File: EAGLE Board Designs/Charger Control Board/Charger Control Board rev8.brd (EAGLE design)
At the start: 86.4 x 101.6 mm, 120 parts, among them K1 RELAY_DPDT, K2 RELAY_DPDT, K3 RELAY_DPDT, U1 LOGICGATE_BUFFER, U100 MCP2562FD, U101 MCP2562FD, U2 ADM8316WBX30, U3 VOLTAGE_REGULATOR_MODULE_OKI-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

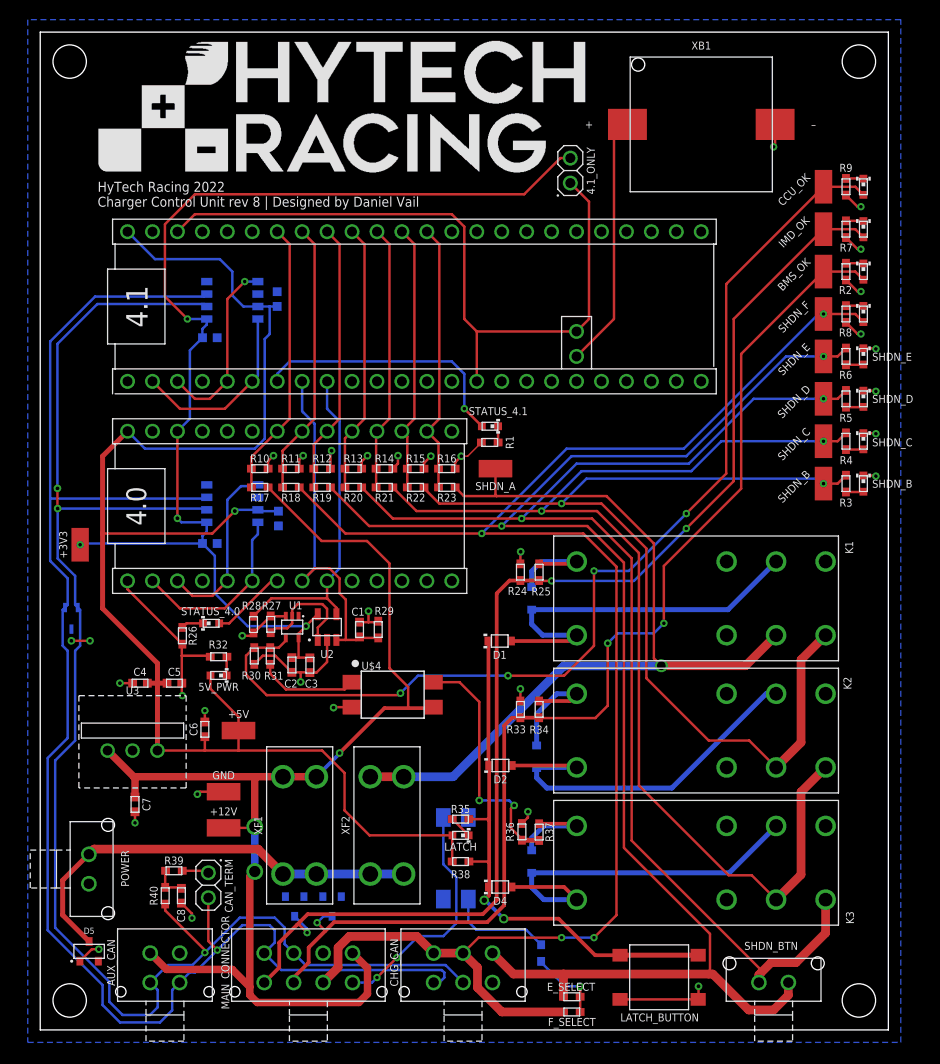
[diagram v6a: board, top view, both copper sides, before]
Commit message: Cleaned up silkscreen
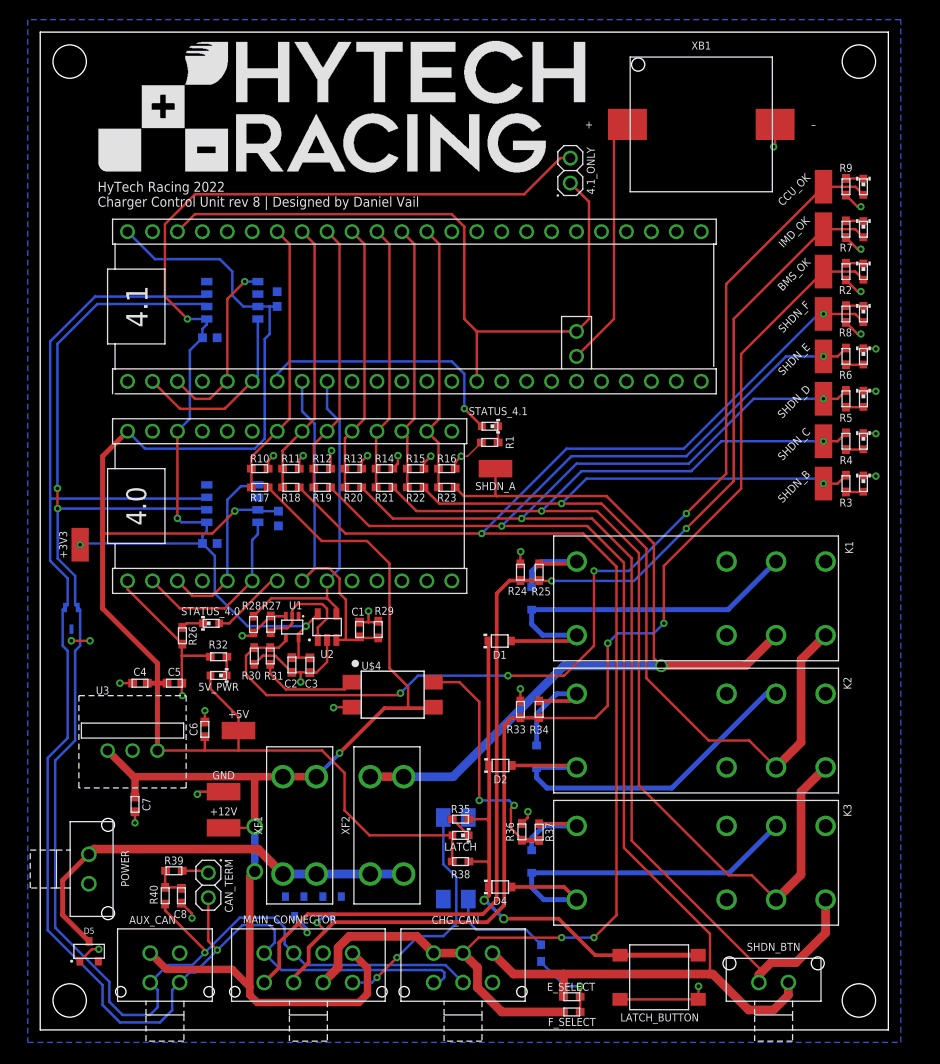
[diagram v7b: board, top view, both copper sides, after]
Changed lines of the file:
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@@
 <drawing>
 <settings>
-<setting alwaysvectorfont="no"/>
+<setting alwaysvectorfont="yes"/>
 <setting verticaltext="up"/>
 </settings>
@@
 <layer number="20" name="Dimension" color="24" fill="1" visible="yes" active="yes"/>
 <layer number="21" name="tPlace" color="7" fill="1" visible="yes" active="yes"/>
-<layer number="22" name="bPlace" color="7" fill="1" visible="no" active="yes"/>
+<layer number="22" name="bPlace" color="7" fill="1" visible="yes" active="yes"/>
 <layer number="23" name="tOrigins" color="15" fill="1" visible="yes" active="yes"/>
 <layer number="24" name="bOrigins" color="15" fill="1" visible="yes" active="yes"/>
 <layer number="25" name="tNames" color="7" fill="1" visible="yes" active="yes"/>
 <layer number="26" name="bNames" color="7" fill="1" visible="yes" active="yes"/>
-<layer number="27" name="tValues" color="7" fill="1" visible="yes" active="yes"/>
+<layer number="27" name="tValues" color="7" fill="1" visible="no" active="yes"/>
 <layer number="28" name="bValues" color="7" fill="1" visible="no" active="yes"/>
 <layer number="29" name="tStop" color="7" fill="3" visible="no" active="yes"/>
@@
 <attribute name="MOPN" value="77-VJ0603Y104JXQPBC" x="130.81" y="32.512" size="1.778" layer="28" rot="MR270" display="off"/>
 <attribute name="MPN" value="VJ0603Y104JXQPW1BC" x="130.81" y="32.512" size="1.778" layer="28" rot="MR270" display="off"/>
-<attribute name="NAME" x="25.92" y="74.422" size="0.8128" layer="26" font="vector" rot="MR270" align="bottom-center"/>
+<attribute name="NAME" x="25.134" y="74.422" size="0.8128" layer="26" font="vector" rot="MR90" align="bottom-center"/>
 <attribute name="TOLERANCE" value="5%" x="130.81" y="32.512" size="1.778" layer="28" rot="MR270" display="off"/>
 <attribute name="VOLTAGE" value="10V" x="130.81" y="32.512" size="1.778" layer="28" rot="MR270" display="off"/>
@@
 <attribute name="MOPN" value="710-885012206012" x="-92.3036" y="-47.2948" size="1.778" layer="27" rot="R270" display="off"/>
 <attribute name="MPN" value="885012206012" x="-92.3036" y="-47.2948" size="1.778" layer="27" rot="R270" display="off"/>
-<attribute name="NAME" x="14.744" y="11.6332" size="0.8128" layer="25" font="vector" rot="R90" align="bottom-center"/>
+<attribute name="NAME" x="14.2748" y="12.204" size="0.8128" layer="25" font="vector" rot="R180" align="bottom-center"/>
 <attribute name="TOLERANCE" value="10%" x="-92.3036" y="-47.2948" size="1.778" layer="27" rot="R270" display="off"/>
 <attribute name="VOLTAGE" value="10V" x="-92.3036" y="-47.2948" size="1.778" layer="27" rot="R270" display="off"/>
@@
 <attribute name="MANUFACTURER" value="MOLEX" x="-22.225" y="89.916" size="1.778" layer="27" rot="R180" display="off"/>
 <attribute name="MPN" value="430450814" x="-22.225" y="89.916" size="1.778" layer="27" rot="R180" display="off"/>
-<attribute name="NAME" x="19.2532" y="6.858" size="0.8128" layer="25" font="vector" rot="R90" align="bottom-center"/>
+<attribute name="NAME" x="25.4" y="10.8458" size="0.8128" layer="25" font="vector" align="bottom-center"/>
 </element>
 <element name="R25" library="HyTechDevices" package="0603-RES" value="RESISTOR_0603_22" x="50.8" y="46.609" smashed="yes" rot="R270">
@@
 <attribute name="MOPN" value="603-RC0603FR-0760R4L" x="119.4054" y="86.0552" size="1.778" layer="27" rot="R90" display="off"/>
 <attribute name="MPN" value="RC0603FR-0760R4L" x="119.4054" y="86.0552" size="1.778" layer="27" rot="R90" display="off"/>
-<attribute name="NAME" x="11.1506" y="13.6652" size="0.8128" layer="25" font="vector" rot="R270" align="bottom-center"/>
+<attribute name="NAME" x="11.9634" y="13.7668" size="0.8128" layer="25" font="vector" rot="R90" align="bottom-center"/>
 <attribute name="POWER" value="0.1W" x="119.4054" y="86.0552" size="1.778" layer="27" rot="R90" display="off"/>
 <attribute name="RESISTANCE" value="60.4" x="119.4054" y="86.0552" size="1.778" layer="27" rot="R90" display="off"/>
@@
 <attribute name="MOPN" value="604-APT1608SECK" x="83.82" y="68.58" size="1.778" layer="27" rot="R270" display="off"/>
 <attribute name="MPN" value="APT1608SECK" x="83.82" y="68.58" size="1.778" layer="27" rot="R270" display="off"/>
-<attribute name="NAME" x="84.709" y="68.5426" size="0.8128" layer="25" font="vector" align="center-left"/>
 </element>
 <element name="R5" library="HyTechDevices" package="0603-RES" value="RESISTOR_0603_1K" x="82.042" y="64.262" smashed="yes" rot="R270">
@@
 <attribute name="MOPN" value="604-APT1608SECK" x="80.01" y="62.992" size="1.778" layer="27" rot="R270" display="off"/>
 <attribute name="MPN" value="APT1608SECK" x="80.01" y="62.992" size="1.778" layer="27" rot="R270" display="off"/>
-<attribute name="NAME" x="84.709" y="64.25" size="0.8128" layer="25" font="vector" align="center-left"/>
 </element>
 <element name="R4" library="HyTechDevices" package="0603-RES" value="RESISTOR_0603_1K" x="82.042" y="59.944" smashed="yes" rot="R270">
@@
 <attribute name="MOPN" value="604-APT1608SECK" x="80.01" y="58.674" size="1.778" layer="27" rot="R270" display="off"/>
 <attribute name="MPN" value="APT1608SECK" x="80.01" y="58.674" size="1.778" layer="27" rot="R270" display="off"/>
-<attribute name="NAME" x="84.709" y="59.8304" size="0.8128" layer="25" font="vector" align="center-left"/>
 </element>
 <element name="R3" library="HyTechDevices" package="0603-RES" value="RESISTOR_0603_1K" x="82.042" y="55.626" smashed="yes" rot="R270">
@@
 <attribute name="MOPN" value="604-APT1608SECK" x="80.01" y="54.356" size="1.778" layer="27" rot="R270" display="off"/>
 <attribute name="MPN" value="APT1608SECK" x="80.01" y="54.356" size="1.778" layer="27" rot="R270" display="off"/>
-<attribute name="NAME" x="84.709" y="55.614" size="0.8128" layer="25" font="vector" align="center-left"/>
 </element>
 <element name="R23" library="HyTechDevices" package="0603-RES" value="RESISTOR_0603_33K" x="41.402" y="55.245" smashed="yes" rot="R180">
@@
 <attribute name="MOPN" value="655-6-1393243-2" x="74.93" y="17.018" size="1.778" layer="27" display="off"/>
 <attribute name="MPN" value="RT424009" x="74.93" y="17.018" size="1.778" layer="27" display="off"/>
-<attribute name="NAME" x="82.042" y="11.43" size="0.8128" layer="25" font="vector" rot="R270" align="bottom-center"/>
+<attribute name="NAME" x="81.788" y="22.352" size="0.8128" layer="25" font="vector" rot="R270" align="bottom-center"/>
 </element>
 <element name="C5" library="HyTechDevices" package="0603-CAP" value="CAPACITOR_0603_10V_1UF" x="13.6652" y="35.306" smashed="yes">
@@
 <attribute name="MANUFACTURER" value="Molex" x="19.05" y="-7.874" size="1.778" layer="27" rot="R180" display="off"/>
 <attribute name="MPN" value="430450414" x="19.05" y="-7.874" size="1.778" layer="27" rot="R180" display="off"/>
-<attribute name="NAME" x="7.62" y="6.858" size="0.8128" layer="25" font="vector" rot="R90" align="bottom-center"/>
+<attribute name="NAME" x="11.43" y="10.795" size="0.8128" layer="25" font="vector" align="bottom-center"/>
 </element>
 <element name="POWER" library="HyTechDevices" package="MOLEX_MICROFIT_PTH_VERTICAL_02_SINGLE" value="CONNECTOR-2_MF_T_V_" x="4.953" y="16.383" smashed="yes" rot="R90">
@@
 <attribute name="MOPN" value="538-43650-0217" x="74.676" y="4.826" size="1.778" layer="27" rot="R180" display="off"/>
 <attribute name="MPN" value="0436500217" x="74.676" y="4.826" size="1.778" layer="27" rot="R180" display="off"/>
-<attribute name="NAME" x="74.422" y="8.9662" size="0.8128" layer="25" font="vector" rot="R180" align="bottom-center"/>
+<attribute name="NAME" x="74.676" y="8.0518" size="0.8128" layer="25" font="vector" align="bottom-center"/>
 </element>
 <element name="U2" library="HyTechDevices_temp" package="SOT-23-5" value="ADM8316WBX30" x="29.21" y="41.021" smashed="yes">
@@
 <attribute name="MANUFACTURER" value="MOLEX" x="43.053" y="4.826" size="1.778" layer="27" rot="R180" display="off"/>
 <attribute name="MPN" value="430450614" x="43.053" y="4.826" size="1.778" layer="27" rot="R180" display="off"/>
-<attribute name="NAME" x="36.449" y="6.858" size="0.8128" layer="25" font="vector" rot="R90" align="bottom-center"/>
+<attribute name="NAME" x="42.291" y="10.795" size="0.8128" layer="25" font="vector" align="bottom-center"/>
 </element>
 <element name="R18" library="HyTechDevices" package="0603-RES" value="RESISTOR_0603_33K" x="25.527" y="55.245" smashed="yes" rot="R180">
@@
 <attribute name="MOPN" value="580-OKI78SR5/1.5W36C" x="9.398" y="28.448" size="1.778" layer="27" display="off"/>
 <attribute name="MPN" value="OKI-78SR-5/1.5-W36-C" x="9.398" y="28.448" size="1.778" layer="27" display="off"/>
-<attribute name="NAME" x="9.398" y="34.163" size="0.8128" layer="25" font="vector" align="bottom-center"/>
+<attribute name="NAME" x="6.35" y="34.163" size="0.8128" layer="25" font="vector" align="bottom-center"/>
 </element>
 <element name="U$3" library="HyTechManufacturing" package="LOGO_HYTECH_LARGE" value="" x="5.842" y="87.376" smashed="yes"/>
@@
 <wire x1="16.256" y1="24.257" x2="16.002" y2="24.003" width="0.254" layer="1"/>
 <via x="16.002" y="24.003" extent="1-16" drill="0.381"/>
-<wire x1="83.82" y1="56.451" x2="83.947" y2="56.578" width="0.254" layer="1"/>
 <wire x1="42.8752" y1="58.42" x2="43.5238" y2="58.42" width="0.1524" layer="1"/>
 <wire x1="43.5238" y1="58.42" x2="44.9208" y2="59.817" width="0.1524" layer="1"/>
@@
 <vertex x="87.63" y="102.87"/>
 </polygon>
-<wire x1="83.82" y1="56.451" x2="85.027" y2="56.451" width="0.254" layer="1"/>
 <wire x1="85.027" y1="56.451" x2="85.09" y2="56.388" width="0.254" layer="1"/>
 <via x="85.09" y="56.388" extent="1-16" drill="0.3556"/>
@@
 <via x="5.969" y="8.2169" extent="1-16" drill="0.381"/>
 <wire x1="4.0386" y1="6.9977" x2="5.2578" y2="8.2169" width="0.254" layer="1"/>
+<wire x1="83.82" y1="56.451" x2="85.027" y2="56.451" width="0.254" layer="1"/>
 </signal>
 <signal name="N$1">

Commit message: Switched R100 to 1k, added input filtering to 5v regulator
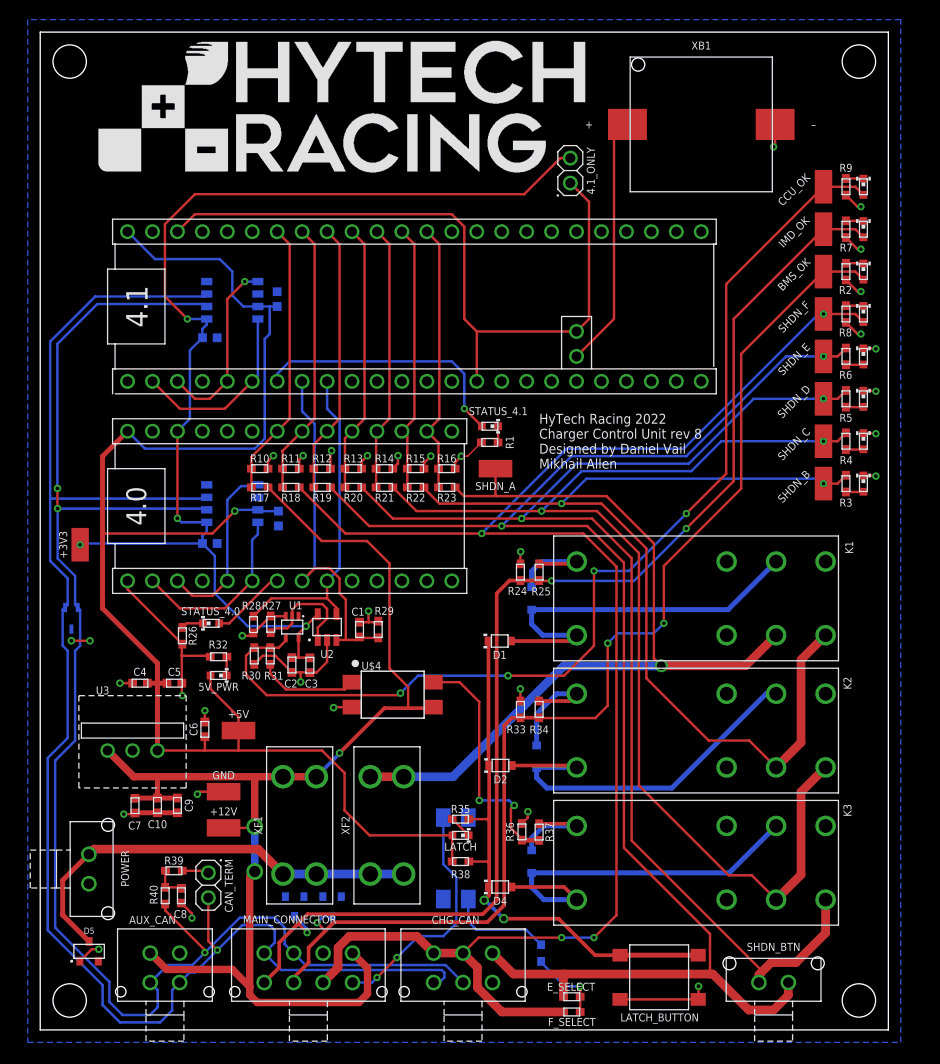
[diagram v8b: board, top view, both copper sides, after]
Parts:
- added C10: CAPACITOR_0603_10V_0.1UF, HyTechDevices:0603-CAP
- added C9: CAPACITOR_0603_10V_1UF, HyTechDevices:0603-CAP
- R100: value RESISTOR_0603_1.33K -> RESISTOR_0603_1K
- moved C7 0.13 mm to (9.65, 22.8)
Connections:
- net +12V: now also C10.2, C9.1
- net GND: now also C10.1, C9.2
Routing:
- net GND: track 94.6 -> 99.0 mm
- net +12V: track 125.2 -> 129.6 mm
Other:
- board text added: "HyTech Racing 2022 Charger Control Unit rev 8 Designed by Daniel Vail Mikhail Allen"
- board text removed: "HyTech Racing 2022 Charger Control Unit rev 8 | Designed by Daniel Vail"
